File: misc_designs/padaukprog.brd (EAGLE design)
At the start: 100 x 100 mm, 126 parts, among them IC1 LM358D, J1 JUMPER_SOLDER_1X2, M1 XT1861B, P1 B3B-PH-K, Q1 BSS84, Q2 8MHz, Q3 BSS84, Q4 BSS123, U1 MIC550X

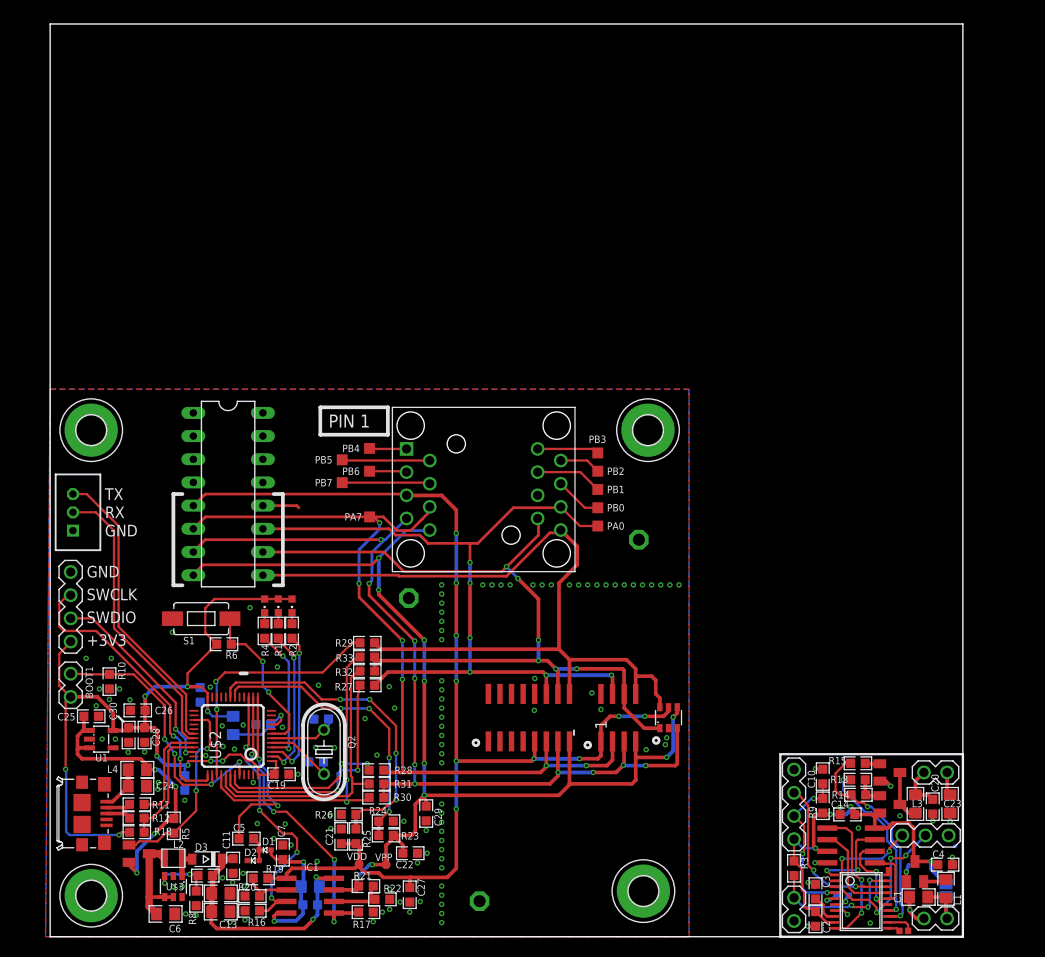
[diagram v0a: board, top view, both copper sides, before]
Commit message: Add minimal STM32F030
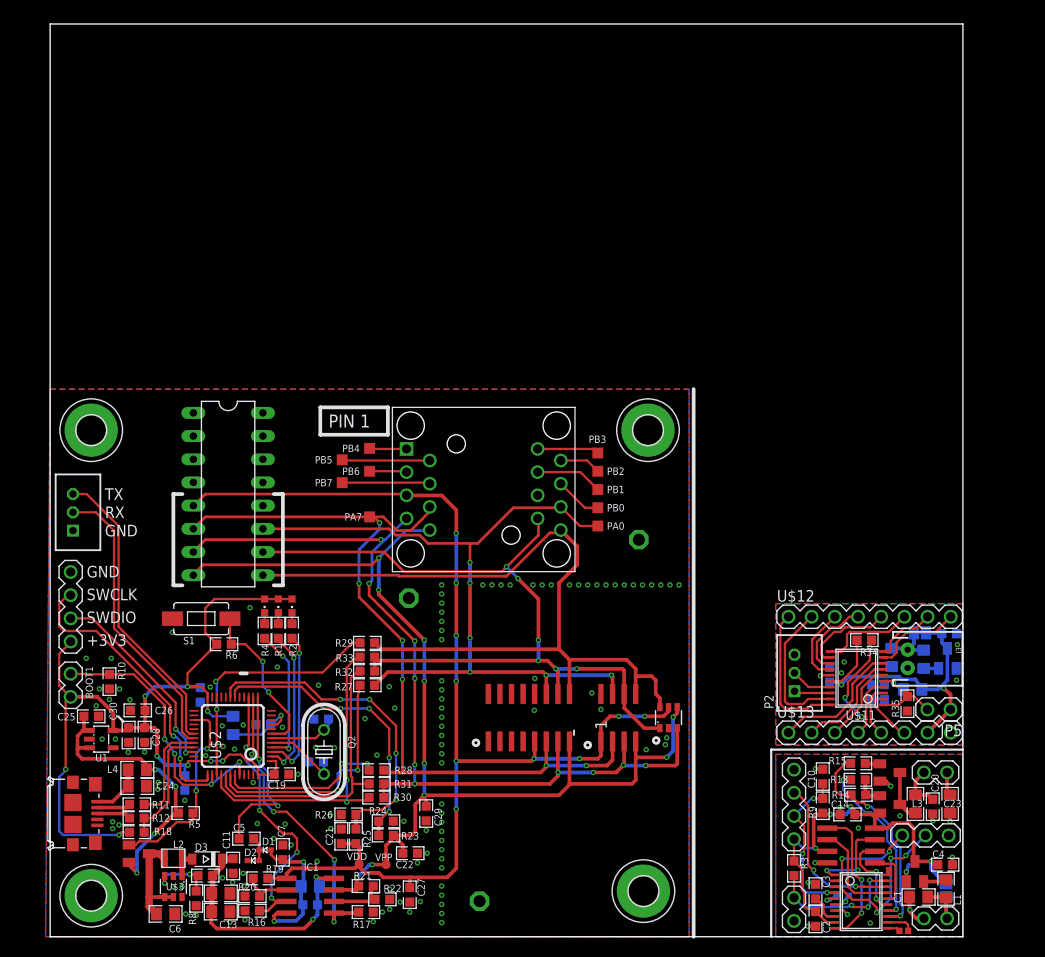
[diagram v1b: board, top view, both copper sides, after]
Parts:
- added C32: 22uF 16V, GadgetFactory:0805
- added C33: 10uF, GadgetFactory:0603
- added C34, C37: 1uF, GadgetFactory:0603
- added C35, C36: 100nF, GadgetFactory:0603
- added J2: JUMPER_SOLDER_1X2, dp_devices:JUMPER_SOLDER_1X2
- added J3: JST-PH 2mm, SparkFun-Connectors:JST-2-PTH
- added JP5: PIN-1X2, alvie:PIN-1X2
- added L6: 10uH, GadgetFactory:0805
- added L7: 600R, GadgetFactory:0805
- added M2: XT1861B, alvie:SOT23
- added P2: B3B-PH-K, con-jst-ph:B3B-PH-K
- added R34, R35: 10K, GadgetFactory:0603
- added U$11: STM32F030F4P6, alvie:TSSOP20
- added U$12, U$13: PIN-1X8, alvie:PIN-1X8
- moved R5 1.91 mm to (14.8, 13.6), turned to 180 degrees
- moved USB1 1.00 mm to (2.50, 13.5)
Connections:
- new net N$10: C34.2, C35.2, L7.1, U$11.5
- new net N$13: C32.2, J2.1, J3.1, L6.1
- new net N$16: L6.2, M2.2
- new net N$23: JP5.2, R35.2, U$11.1
- new net PA0: U$11.6, U$13.3
- new net PA1: U$11.7, U$13.2
- new net PA10: P2.1, U$11.18
- new net PA13: U$11.19, U$12.2
- new net PA14: U$11.20, U$12.1
- new net PA2: U$11.8, U$13.1
- new net PA3: U$11.9, U$12.8
- new net PA4: U$11.10, U$12.7
- new net PA5: U$11.11, U$12.6
- new net PA6: U$11.12, U$12.5
- new net PA7: U$11.13, U$12.4
- new net PA9: P2.2, U$11.17
- new net PB1: U$11.14, U$12.3
- new net PF0: U$11.2, U$13.6
- new net PF1: U$11.3, U$13.5
- new net XNRST: C37.2, R34.1, U$11.4, U$13.4
- net +3V3: now also C33.2, C36.2, J2.2, JP5.1, L7.2, M2.3, R34.2, U$11.16, U$13.7
- net GND: now also C32.1, C33.1, C34.1, C35.1, C36.1, C37.1, J3.2, M2.1, P2.3, R35.1, U$11.15, U$13.8
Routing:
- net +3V3: track 234.3 -> 270.7 mm, vias 13 -> 15
- net XNRST: track 0.00 -> 19.3 mm, vias 0 -> 3
- net PA13: track 0.00 -> 15.8 mm
- net PA14: track 0.00 -> 15.8 mm
- net PA2: track 0.00 -> 14.6 mm
- net PA1: track 0.00 -> 11.8 mm
- net PA5: track 0.00 -> 10.4 mm
- net PA6: track 0.00 -> 10.0 mm
- net PA3: track 0.00 -> 9.86 mm
- net PA7: track 0.00 -> 9.16 mm
- net PA0: track 0.00 -> 9.05 mm
- net PB1: track 0.00 -> 8.33 mm
- net PA4: track 0.00 -> 6.99 mm
- net PF0: track 0.00 -> 6.03 mm
- net PF1: track 0.00 -> 5.92 mm
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
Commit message: Cleanup
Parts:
- moved C32 1.50 mm to (92.2, 32.1)
- moved C33 0.20 mm to (98.3, 33.2)
- moved M2 0.10 mm to (98.2, 30.5)
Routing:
- net +3V3: track 270.7 -> 282.4 mm
- net GND: track 34.0 -> 44.6 mm, vias 141 -> 147
- net N$10: track 2.71 -> 5.19 mm
- net N$13: track 5.72 -> 6.77 mm

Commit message: Updates
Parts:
- removed TP1, TP10, TP2, TP3, TP4, TP5, TP6, TP7, TP8, TP9: TPTP12SQ, testpad:TP12SQ
- added BOOT2, JP7: PIN-1X2, alvie:PIN-1X2
- added C38, C39: 16pF 6.3V, GadgetFactory:0603
- added C40, C41, C42, C43, C45: 100nF 6.3V, GadgetFactory:0603
- added C44, C46: 10uF, GadgetFactory:0603
- added C47, C52: 20pF 6.3V, GadgetFactory:0603
- added C48, C49, C55: 10uF, GadgetFactory:0805
- added C50, C53, C54, C57, C58, C59, C60, C61, C93, C94, C95: 100nF, GadgetFactory:0603
- added C51, C56: 10nF, GadgetFactory:0603
- added C96: 2.2uF, GadgetFactory:0805
- added C97: 1uF, GadgetFactory:0603
- added C98: 1nF, GadgetFactory:0603
- added C99: 100nF/DNP, GadgetFactory:0603
- added D4: 1N4148W, alvie:SOD-123
- added H5, H7, H8: MOUNT-PAD-ROUND3.2, holes:3,2-PAD
- added IC11: LAN8720A, sigedi-footprints:QFN24_4MM_X_4MM
- added IC15: TPS62063, alvie:WSON8-2.1X2.1
- added J4: (no value), GadgetFactory:SPC4078-NOSLOT
- added L10, L12, L9: 600R, GadgetFactory:0805
- added L11: DFE252012F, alvie:L2520
- added L8: 10mH, GadgetFactory:0805
- added LED4, LED5, LED6: LG L29K-G2J1-24, dp_devices:LED-603
- added Q5: 25MHz, crystal:HC49U-V
- added Q6: FDN338, transistor-power:SUPER-SOT3
- added Q7: 8MHz, crystal:HC49U-V
- added R36, R37, R39, R40: 20R, GadgetFactory:0603
- added R38, R43, R50, R78: 10K, GadgetFactory:0603
- added R41, R42, R53, R54, R55, R57, R60: 0R, GadgetFactory:0603
- added R44: 100K, GadgetFactory:0603
- added R45, R46, R47, R79, R80: 2K2, GadgetFactory:0603
- added R48, R49: 2K2/DNP, GadgetFactory:0603
- added R51: 1K5/DNP, GadgetFactory:0603
- added R52: 470K, GadgetFactory:0603
- added R56, R61: 0R/DNP, GadgetFactory:0603
- added R58, R59: 330R, GadgetFactory:0603
- added R82: 12K1, GadgetFactory:0603
- added R83, R84, R85, R86: 49R9, GadgetFactory:0603
- added S2, S3: SWITCHES_-SMD-1101NE, EAGLE_BoosterPack_Library:TACTILE-SWITCH-1101NE
- added SV1: (no value), con-lstb:MA13-2W
- added T2: Hanrun HR917550A, alvie:HR13550A
- added TP20, TP21, TP22, TP23, TP24, TP25, TP26, TP27, TP28, TP29: TPTP12SQ, testpad:TP12SQ
- added U$14: PN532_NFCB, alvie:HW-147-NFC-NOHOLES
- added U$15: STM32F070F6, alvie:TSSOP20
- added U$16: MIC550X, alvie:SOT23-5L
- added U$17: PIN-1X4, alvie:PIN-1X4
- added U2: STM32F107RCT6, ST Microelctronics_By_element14_Batch_1:QFP50P1200X1200X160-64N
- added U3: ESP-WROOM-32, esp32:ESP-WROOM-32
- added USB2, USB3: CON-USB-F-MICRO-B, dp_devices:CONN_USB_MICRO-B
- U$10: value SOP-16-1.27 -> PIN-1X4; device alvie:SOP-16-1.27 -> alvie:PIN-1X4
- moved IC2 30.2 mm to (48.5, 40.0), turned to 0 degrees
- moved TP12 14.8 mm to (26.1, 43.9)
- moved U$10 12.6 mm to (35.5, 53.0), turned to 180 degrees
- moved P1 11.9 mm to (14.0, 43.5), turned to 270 degrees
- moved H1 9.55 mm to (66.5, 46.0)
- moved H3 9.55 mm to (3.50, 46.0)
- moved TP11 9.06 mm to (65.5, 34.5)
- moved U$7 7.57 mm to (63.2, 16.5)
- moved U$8 7.57 mm to (68.8, 16.5)
- moved U$9 7.57 mm to (53.5, 16.6)
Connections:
- removed net N$34: TP2.TP, U$10.2
- removed net N$38: TP3.TP, U$10.3
- removed net N$41: TP4.TP, U$10.4
- removed net N$47: TP9.TP, U$10.16
- removed net N$48: TP8.TP, U$10.15
- removed net N$49: TP7.TP, U$10.14
- removed net N$52: TP6.TP, U$10.13
- new net ESP_EN: U2.49, U3.3
- new net ESP_IO0: U2.53, U3.25
- new net ESP_MISO: R56.2, R57.2, U3.31
- new net ESP_MOSI: R60.2, R61.2, U3.37
- new net ESP_ON: Q6.1, R44.2
- new net ESP_RX: U2.51, U3.34
- new net ESP_SCK: R55.2, U3.30
- new net ESP_TX: U2.52, U3.35
- new net ESP_VCC: Q6.3, U3.2
- new net MCO: R53.1, U2.41
- new net N$17: L12.1, USB3.P1
- new net N$20: R39.1, USB2.P2
- new net N$22: R40.1, USB2.P3
- new net N$24: R42.1, USB2.P4
- new net N$25: R54.2, U3.29
- new net N$26: LED4.C, R45.1
- new net N$27: LED5.C, R46.1
- new net N$28: LED6.C, R47.1
- new net N$29: R36.1, USB3.P2
- new net N$30: IC2.16, TP23.TP
- new net N$31: IC2.15, TP22.TP
- new net N$32: IC2.14, TP21.TP
- new net N$35: IC2.13, TP20.TP
- new net N$39: L9.1, USB2.P1
- new net N$40: IC11.24, R82.2
- new net N$44: C57.1, T2.5
- new net N$45: C58.1, T2.4
- new net N$46: R58.1, T2.12
- new net N$53: R59.1, T2.9
- new net N$54: IC2.1, TP24.TP
- new net N$55: IC2.2, TP25.TP
- new net N$56: C99.2, L10.2, R83.2, R84.2, R85.2, R86.2
- new net N$57: IC2.3, TP26.TP
- new net N$58: C97.2, C98.2, IC11.6
- new net N$59: IC2.4, TP27.TP
- new net NBOOT0: BOOT2.1, R38.2, U$15.1
- new net NIRQ: U$14.IRQ, U$15.7
- new net NLED0: R45.2, U2.46
- new net NLED1: R46.2, U2.35
- new net NLED2: R47.2, U2.36
- new net NNRST: R43.1, S3.P$1, U$15.4
- new net NOSC_IN: C47.2, Q7.2, U$15.2
- new net NOSC_OUT: C52.2, Q7.1, U$15.3
- new net NRSTO: U$14.RSTO, U$15.6
- new net NSWCLK: U$15.20, U$17.3
- new net NSWDIO: U$15.19, U$17.2
- new net NUSBDM: R36.2, U$15.17
- new net NUSBDP: R37.2, R51.1, U$15.18
- new net N_MISO: U$14.MISO, U$15.12
- new net N_MOSI: U$14.MOSI, U$15.13
- new net N_RX: U$14.SDA/TX, U$15.9
- new net N_SCK: U$14.SCK, U$15.11
- new net N_SS: U$14.SS, U$15.10
- new net N_TX: U$14.SCL/RX, U$15.8
- new net PA15/NSS: R54.1, U2.50
- new net PA3/ADC3: SV1.9, U2.17
- new net PA4/DAC1: SV1.7, U2.20
- new net PA5/DAC2: SV1.8, U2.21
- new net PB6/UART1_TX: SV1.24, U2.58
- new net PB7/UART1_RX: SV1.23, U2.59
- new net PHY_LED0: IC11.3, T2.10
- new net PHY_LED1: IC11.2, T2.11
- new net REG33IN: C49.2, D4.1, IC15.5, IC15.7, IC15.8, J4.3, SV1.2
- new net RMII_CRS_DV: IC11.11, U2.23
- new net RMII_MDC: IC11.13, R79.1, U2.9
- new net RMII_MDIO: IC11.12, R80.1, U2.16
- new net RMII_NRST: IC11.15, R78.1, U2.22
- new net RMII_REF_CLK: IC11.14, U2.15
- new net RMII_RXD0: IC11.8, U2.24
- new net RMII_RXD1: IC11.7, U2.25
- new net RMII_TXD0: IC11.17, U2.33
- new net RMII_TXD1: IC11.18, U2.34
- new net RMII_TX_EN: IC11.16, U2.30
- new net RXM1: IC11.20, R84.1, T2.2
- new net RXP1: IC11.21, R83.1, T2.1
- new net SHIELD: T2.8, T2.Z1, T2.Z2
- new net TXM1: IC11.22, R86.1, T2.6
- new net TXP1: IC11.23, R85.1, T2.3
- new net USBID/UART1RX: R42.2, U2.43
- new net USBPWR: D4.2, L9.2, R41.1
- new net USBPWR1: C55.2, L12.2, U$16.1, U$16.3
- new net VBUSDET/UART1TX: R41.2, U2.42
- new net XBOOT0: JP7.1, R50.1, U2.60
- new net XI: IC11.5, R53.2
- new net XOSC_IN: C38.2, Q5.2, U2.5
- new net XOSC_OUT: C39.2, Q5.1, U2.6
- new net XPA0: SV1.12, U2.14
- new net XPB0/ADC8: SV1.10, U2.26
- new net XPB1: SV1.5, U2.27
- new net XPB2: SV1.6, U2.28
- new net XPC0: SV1.13, U2.8
- new net XPC13: SV1.22, U2.2
- new net XPC14: SV1.19, U2.3
- new net XPC15: SV1.20, U2.4
- new net XPC2: SV1.14, U2.10
- new net XPC3: SV1.11, U2.11
- new net XPC6: SV1.15, U2.37
- new net XPC7: SV1.16, U2.38
- new net XPC8: SV1.17, U2.39
- new net XPC9: SV1.18, U2.40
- new net XPD2: SV1.21, U2.54
- new net XSCL: R48.1, SV1.26, U$10.3, U2.61
- new net XSDA: R49.1, SV1.25, U$10.4, U2.62
- new net XSPI_MISO: R57.1, R61.1, U2.56
- new net XSPI_MOSI: R56.1, R60.1, U2.57
- new net XSPI_SCK: R55.1, U2.55
- new net XSW: IC15.2, L11.P$1
- new net XUSBDM: R39.2, U2.44
- new net XUSBDP: R40.2, U2.45
- new net XVDDA: C40.1, C44.2, L8.2, U2.13
- new net XXNRST: R52.2, S2.P$2, U2.7
- net +3V3: now also BOOT2.2, C41.1, C42.1, C43.1, C45.1, C46.2, C48.2, C50.2, C51.2, C53.2, C54.2, C56.2, C59.2, C60.2, C61.2, C93.2, C94.2, C95.2, C96.2, IC11.1, IC11.19, IC11.9, IC15.4, JP7.2, L10.1, L11.P$2, L8.1, LED4.A, LED5.A, LED6.A, Q6.2, R43.2, R44.1, R48.2, R49.2, R51.2, R52.1, R58.2, R59.2, R78.2, R79.2, R80.2, SV1.1, U$10.2, U$14.VCC, U$14.VCC1, U$15.16, U$15.5, U$16.5, U$17.1, U2.1, U2.19, U2.32, U2.48, U2.64
- net GND: now also C38.1, C39.1, C40.2, C41.2, C42.2, C43.2, C44.1, C45.2, C46.1, C47.1, C48.1, C49.1, C50.1, C51.1, C52.1, C53.1, C54.1, C55.1, C56.1, C57.2, C58.2, C59.1, C60.1, C61.1, C93.1, C94.1, C95.1, C96.1, C97.1, C98.1, C99.1, IC11.P, IC15.1, IC15.3, IC15.6, IC15.EXP, J4.1, R38.1, R50.2, R82.1, S2.P$1, S3.P$2, SV1.3, SV1.4, U$10.1, U$14.GND, U$14.GND1, U$15.15, U$16.2, U$17.4, U2.12, U2.18, U2.31, U2.47, U2.63, U3.1, U3.15, U3.38, U3.GND, USB2.P5, USB3.P5; no longer U$10.12
- net MCU_MISO: no longer U$10.7
- net MCU_MOSI: no longer U$10.10
- net MCU_PA0: now also TP28.TP; no longer TP10.TP, U$10.11
- net MCU_PA7: now also TP29.TP; no longer TP5.TP, U$10.6
- net MCU_SCK: no longer U$10.9
- net N$33: now also R37.1, USB3.P3; no longer TP1.TP, U$10.1
- net VDD_OUT: no longer U$10.5
- net VPP_OUT: no longer U$10.8
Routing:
- net +3V3: track 282.4 -> 604.2 mm, vias 15 -> 43
- net REG33IN: track 0.00 -> 102.1 mm, vias 0 -> 4
- net GND: track 44.6 -> 107.9 mm, vias 147 -> 257
- net SHIELD: track 0.00 -> 46.7 mm
- net XXNRST: track 0.00 -> 38.5 mm, vias 0 -> 4
- net RMII_MDC: track 0.00 -> 37.9 mm, vias 0 -> 2
- net VDD_OUT: track 127.1 -> 90.1 mm, vias 10 -> 8
- net ESP_EN: track 0.00 -> 36.9 mm, vias 0 -> 3
- net RMII_REF_CLK: track 0.00 -> 36.7 mm
- net XPD2: track 0.00 -> 35.4 mm, vias 0 -> 6
- net NNRST: track 0.00 -> 34.4 mm, vias 0 -> 2
- net XSCL: track 0.00 -> 34.2 mm, vias 0 -> 2
- net ESP_TX: track 0.00 -> 32.6 mm, vias 0 -> 3
- net XSDA: track 0.00 -> 32.6 mm, vias 0 -> 1
- net ESP_MOSI: track 0.00 -> 31.8 mm, vias 0 -> 3
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- added copper zone on layer 1, net +3V3
- added copper zone on layer 1, net REG33IN
- added copper zone on layer 1, net XSW
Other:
- board text added: "SWCK"
- board text added: "SWD"
- board text added: "VCC"
- board text removed: "PIN 1"

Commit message: Rotate design
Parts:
- moved C60 22.6 mm to (92.0, 63.6), turned to 0 degrees
- moved Q7 20.4 mm to (85.5, 61.5), turned to 0 degrees
- moved S3 19.9 mm to (97.5, 59.5), turned to 270 degrees
- moved C52 19.1 mm to (84.0, 60.0), turned to 0 degrees
- moved C47 17.8 mm to (87.0, 60.0), turned to 180 degrees
- moved R43 17.6 mm to (94.6, 59.2), turned to 270 degrees
- moved BOOT2 16.1 mm to (97.0, 39.0), turned to 0 degrees
- moved C55 14.4 mm to (98.6, 42.7), turned to 270 degrees
- moved U$17 13.2 mm to (88.5, 57.0), turned to 180 degrees
- moved USB3 12.3 mm to (98.0, 50.5), turned to 90 degrees
- moved C61 11.7 mm to (82.1, 44.6), turned to 90 degrees
- moved R38 11.6 mm to (92.5, 40.0), turned to 0 degrees
- moved U$16 10.5 mm to (95.5, 43.0), turned to 90 degrees
- moved R51 8.08 mm to (92.0, 53.0), turned to 0 degrees
- moved C59 7.76 mm to (92.5, 43.0), turned to 270 degrees
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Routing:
- net +3V3: track 604.2 -> 614.9 mm
- net GND: track 107.9 -> 111.4 mm, vias 257 -> 266

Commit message: Wip for Zigbee
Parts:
- added C62, C63, C64: (no value), GadgetFactory:0603
- added C65, C69, C83: (no value), GadgetFactory:0805
- added C66: 22uF 16V, GadgetFactory:0805
- added C67: 10uF, GadgetFactory:0603
- added C68, C75: 100nF, GadgetFactory:0603
- added C70, C71, C72, C73, C74, L14, L15: (no value), GadgetFactory:0402
- added C76, C82: 1uF, GadgetFactory:0603
- added C77, C78, C80, C81: 100nF, GadgetFactory:0402
- added C79: 220pF, GadgetFactory:0402
- added C84, C85, C86, C87: 15pF, GadgetFactory:0402
- added IC4, IC5: 4051D, 40xx:SO16
- added IC6: IC_DIL16-SOIC-16, dp_devices:SOIC-16
- added J5: AVR_SPI_PRG_6NS, SparkFun-Connectors:2X3-NS
- added J6: JST-PH 2mm, SparkFun-Connectors:JST-2-PTH@1
- added J7: CON-HIROSE-COAXIAL-U.FL, m-pad-2.1:CON-U.FL
- added JP10, JP8, U$26: PIN-1X8, alvie:PIN-1X8
- added JP11: PIN-1X2, alvie:PIN-1X2
- added JP6: VBat +, alvie:PIN-1X2
- added JP9: Pedal, alvie:PIN-1X2
- added L13: 10uH, GadgetFactory:0805
- added L16: 600R, GadgetFactory:0805
- added LED7, LED8: LG L29K-G2J1-24, dp_devices:LED-603
- added M3: XT1861B, alvie:SOT23
- added Q10, Q11, Q8, Q9: BSS84, transistor-small-signal:SOT23
- added Q12, Q13: CRISTAL-3225, alvie:CRYSTAL-3225
- added R62, R63, R64, R65, R66, R87: 10K, GadgetFactory:0603
- added R67, R68, R69, R70, R71, R72, R73, R74: 330R, GadgetFactory:0603
- added R75: 56K, GadgetFactory:0603
- added R76: 0R, GadgetFactory:0603
- added R77, R81: 2K2, GadgetFactory:0603
- added SJ1: SOLDERJUMPERNC, headers:SJ_2S_SMALL
- added U$24: (no value), logos:FIKALAB-25X5
- added U$25: SR410361N, alvie:LCD_7SEG_4DIGIT
- added U$27: TSSOP16, alvie:TSSOP16
- added U$28: PFS154-S16, alvie:SOIC16-N
- added U$29, U$31, U$32, U$33: PIN-1X4, alvie:PIN-1X4
- added U$30: CC2530, alvie:RHA-S-PVQFN-N40
- added U4: ATTINY24A-SSU, Atmel_By_element14_Batch_1-00:SOIC127P600X175-14N
- J3: device SparkFun-Connectors:JST-2-PTH -> SparkFun-Connectors:JST-2-PTH@1
- SV1: value (none) -> MA13-2W; device con-lstb:MA13-2W -> alvie:MA13-2W
- U$7: value PMS150C-S08 -> PIN-1X8; device alvie:SOP08 -> alvie:PIN-1X8
- moved H8 57.8 mm to (103.5, 59.5)
- moved R41 45.7 mm to (51.5, 73.0), turned to 90 degrees
- moved R42 37.0 mm to (46.0, 76.5)
- moved C46 23.6 mm to (18.5, 99.0), turned to 180 degrees
- moved U$8 19.1 mm to (51.5, 24.8), turned to 90 degrees
- moved TP11 18.7 mm to (60.5, 16.5)
- moved SV1 17.4 mm to (60.0, 67.0)
- moved H7 13.0 mm to (59.0, 96.5)
- moved H1 7.50 mm to (59.0, 46.0)
- moved U$7 6.52 mm to (64.8, 10.2), turned to 90 degrees
- moved H2 6.24 mm to (58.9, 3.70)
- moved R79 6.18 mm to (35.1, 88.3), turned to 270 degrees
- moved R80 5.66 mm to (33.7, 88.3), turned to 270 degrees
- moved IC2 3.81 mm to (44.7, 40.0)
- moved TP20 3.81 mm to (43.4, 46.7)
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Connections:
- removed net USBID/UART1RX: R42.2, U2.43
- removed net VBUSDET/UART1TX: R41.2, U2.42
- removed net XPC8: SV1.17, U2.39
- removed net XPC9: SV1.18, U2.40
- removed net XPD2: SV1.21, U2.54
- new net +3V3_CC: C75.2, C76.2, C77.2, C78.2, C79.2, C80.2, C81.2, C83.2, L16.2, R87.1, U$30.10, U$30.21, U$30.24, U$30.27, U$30.28, U$30.29, U$30.31, U$30.39, U$31.4
- new net A_MISO: J5.1, U4.8
- new net A_MOSI: J5.4, U4.7
- new net A_RESET: J5.5, U4.4
- new net A_SCK: J5.3, U4.9
- new net CA0: Q8.1, R63.1, U$28.7
- new net CA1: Q9.1, R64.1, U$28.6
- new net CA2: Q10.1, R65.1, U$28.4
- new net CA3: Q11.1, R66.1, U$28.3
- new net CCLED1: R77.2, U$30.11
- new net CCLED2: R81.2, U$30.9
- new net CC_MISO: R76.2, U$30.37
- new net CC_MOSI: R42.2, U$30.38
- new net CC_RST: R87.2, U$30.20, U2.39
- new net CC_RX: U$30.17, U2.53
- new net CC_SCK: R41.2, U$30.5
- new net CC_SS: U$30.6, U2.40
- new net CC_TX: U$30.16, U2.54
- new net DEBUG_C: U$30.34, U$31.2
- new net DEBUG_D: U$30.35, U$31.3
- new net LCLK: U$28.11, U$29.2
- new net LDAT: U$28.13, U$29.3
- new net N$100: IC6.13, U$26.5, U$27.12
- new net N$101: IC6.14, U$26.6, U$27.11
- new net N$102: IC6.12, U$26.4, U$27.13
- new net N$103: IC6.11, U$26.3, U$27.14
- new net N$104: IC6.10, U$26.2, U$27.15
- new net N$105: IC6.9, U$26.1, U$27.16
- new net N$106: C85.2, Q12.1, U$30.32
- new net N$34: IC4.3, IC5.3
- new net N$38: IC4.4, JP8.1
- new net N$41: C66.2, J6.1, L13.1
- new net N$47: L13.2, M3.2
- new net N$48: C67.2, JP11.1, M3.3
- new net N$49: IC5.13, JP10.8
- new net N$52: IC4.13, JP8.8
- new net N$60: IC4.14, JP8.7
- new net N$61: IC4.12, JP8.5
- new net N$62: IC4.1, JP8.4
- new net N$63: IC4.5, JP8.3
- new net N$64: IC4.2, JP8.2
- new net N$65: Q9.3, U$25.9
- new net N$66: J5.2, SJ1.2
- new net N$67: IC5.14, JP10.7
- new net N$68: IC5.15, JP10.6
- new net N$69: IC5.12, JP10.5
- new net N$70: IC4.15, JP8.6
- new net N$71: IC5.1, JP10.4
- new net N$72: IC5.5, JP10.3
- new net N$73: IC5.2, JP10.2
- new net N$74: IC5.4, JP10.1
- new net N$75: Q10.3, U$25.8
- new net N$76: Q8.3, U$25.12
- new net N$77: Q11.3, U$25.6
- new net N$78: C70.1, U$30.26
- new net N$79: C70.2, C73.2, L15.1
- new net N$80: C71.1, U$30.25
- new net N$81: IC6.8, U$27.1, U$7.1
- new net N$82: C71.2, C72.2, L14.1
- new net N$83: C73.1, C74.2, L14.2
- new net N$84: C74.1, J7.S
- new net N$85: R75.2, U$30.30
- new net N$86: C82.2, U$30.40
- new net N$87: LED8.C, R81.1
- new net N$88: C86.2, Q13.3, U$30.23
- new net N$89: C87.2, Q13.1, U$30.22
- new net N$90: C84.2, Q12.3, U$30.33
- new net N$91: IC6.7, U$27.2, U$7.2
- new net N$92: IC6.6, U$27.3, U$7.3
- new net N$93: IC6.5, U$27.4, U$7.4
- new net N$94: IC6.4, U$27.5, U$7.5
- new net N$95: IC6.3, U$27.6, U$7.6
- new net N$96: IC6.2, U$27.7, U$7.7
- new net N$97: IC6.1, U$27.8, U$7.8
- new net N$98: IC6.16, U$26.8, U$27.9
- new net N$99: IC6.15, U$26.7, U$27.10
- new net PEDAL: JP9.2, R62.1, U4.5
- new net SA: R67.2, U$25.11
- new net SB: R68.2, U$25.7
- new net SC: R69.2, U$25.4
- new net SD: R70.2, U$25.2
- new net SDP: R74.2, U$25.3
- new net SE: R71.2, U$25.1
- new net SEG_A: R67.1, U$28.9
- new net SEG_B: R68.1, U$28.14
- new net SEG_C: R69.1, U$28.2
- new net SEG_D: R70.1, U$28.15
- new net SEG_DP: R74.1, U$28.16
- new net SEG_E: R71.1, U$28.10
- new net SEG_F: R72.1, U$28.8
- new net SEG_G: R73.1, U$28.1
- new net SEL_A0: IC5.11, U4.10
- new net SEL_A1: IC4.11, U4.13
- new net SEL_B0: IC5.10, U4.6
- new net SEL_B1: IC4.10, U4.12
- new net SEL_C0: IC5.9, U4.2
- new net SEL_C1: IC4.9, U4.11
- new net SEL_INH: IC4.6, IC5.6, U4.3
- new net SF: R72.2, U$25.10
- new net SG: R73.2, U$25.5
- new net UART1RX: SV1.18, U2.43
- new net UART1TX: SV1.17, U2.42
- new net V_BATT: C62.1, C63.1, C64.1, C65.2, IC4.16, IC5.16, JP6.2, R62.2, SJ1.1, U4.1
- net +3V3: now also C68.2, C69.2, L16.1, LED7.A, LED8.A, Q10.2, Q11.2, Q8.2, Q9.2, R63.2, R64.2, R65.2, R66.2, U$28.5, U$29.4, U$33.1
- net ESP_IO0: now also U2.29; no longer U2.53
- net ESP_MISO: now also R76.1
- net ESP_MOSI: now also R42.1
- net ESP_SCK: now also R41.1
- net GND: now also C62.2, C63.2, C64.2, C65.1, C66.1, C67.1, C68.1, C69.1, C72.1, C75.1, C76.1, C77.1, C78.1, C79.1, C80.1, C81.1, C82.1, C83.1, C84.1, C85.1, C86.1, C87.1, IC4.7, IC4.8, IC5.7, IC5.8, J5.6, J6.2, J7.GND@0, JP11.2, JP6.1, JP9.1, L15.2, M3.1, Q12.2, Q12.4, Q13.2, Q13.4, R75.1, U$28.12, U$29.1, U$30.1, U$30.2, U$30.3, U$30.4, U$30.EXP, U$31.1, U$32.1, U4.14; no longer U$7.8
- net MCU_MISO: no longer U$7.3
- net MCU_MOSI: no longer U$7.6
- net MCU_PA0: no longer U$7.7
- net MCU_PA7: no longer U$7.2
- net MCU_SCK: no longer U$7.5
- net N$24: now also LED7.C, R77.1; no longer R42.1, USB2.P4
- net PA3/ADC3: now also U$33.2; no longer SV1.9
- net PA4/DAC1: now also U$33.3; no longer SV1.7
- net PA5/DAC2: now also U$32.3; no longer SV1.8
- net USBPWR: no longer R41.1
- net VDD_OUT: no longer U$7.1
- net VPP_OUT: no longer U$7.4
- net XPB0/ADC8: now also U$32.2; no longer SV1.10
- net XPB1: now also U$33.4; no longer SV1.5
- net XPB2: now also U$32.4; no longer SV1.6
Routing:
- net +3V3: track 614.9 -> 695.3 mm, vias 43 -> 40
- net +3V3_CC: track 0.00 -> 52.2 mm, vias 0 -> 8
- net V_BATT: track 0.00 -> 46.9 mm, vias 0 -> 5
- net XPD2: track 35.4 -> 0.00 mm, vias 6 -> 0
- net REG33IN: track 102.1 -> 67.5 mm
- net UART1RX: track 0.00 -> 31.6 mm, vias 0 -> 2
- net SEL_INH: track 0.00 -> 29.2 mm, vias 0 -> 4
- net UART1TX: track 0.00 -> 29.0 mm, vias 0 -> 1
- net GND: track 111.4 -> 139.0 mm, vias 266 -> 351
- net CA3: track 0.00 -> 25.1 mm, vias 0 -> 2
- net DEBUG_C: track 0.00 -> 24.2 mm
- net VBUSDET/UART1TX: track 23.9 -> 0.00 mm
- net USBID/UART1RX: track 23.6 -> 0.00 mm, vias 2 -> 0
- net CA1: track 0.00 -> 23.4 mm
- net XPC9: track 23.3 -> 0.00 mm, vias 2 -> 0
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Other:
- board text added: "+"
- board text added: "BATT"
- board text added: "CLK"
- board text added: "CN1"
- board text added: "CN2"
- board text added: "DAT"
- board text added: "JP"
- board text added: "PEDAL"
- board text added: "SOIC16"
- board text added: "TSSOP16"
